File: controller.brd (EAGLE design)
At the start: 100 x 80 mm, 48 parts, among them IC1 7805DT, Q2 MOSFET-NCHANNELBSS123LT1G, Q3 MOSFET-NCHANNELFDD8780, Q5 MMBT4403, SW1 ROT_ENCODER, U1 ATMEGA328P, Y1 16MHz

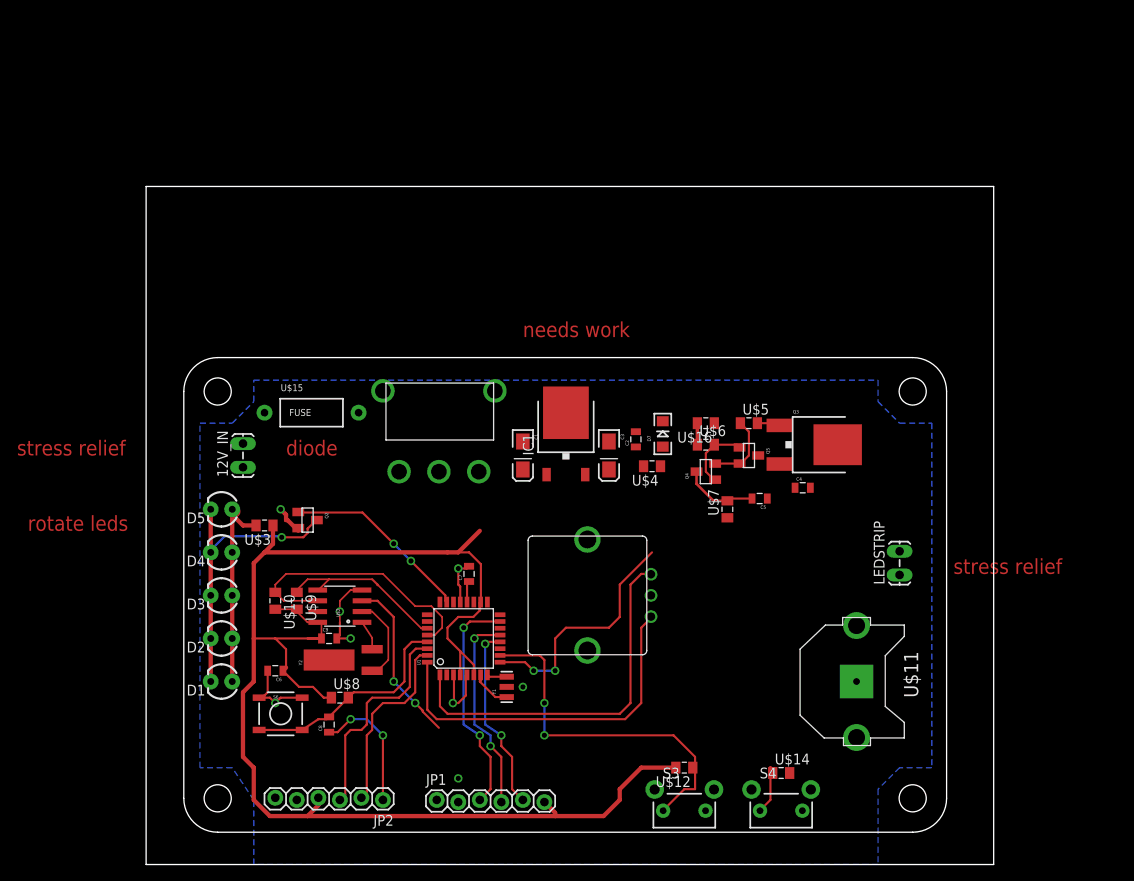
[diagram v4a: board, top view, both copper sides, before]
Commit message: began moving controller to smaller board size.
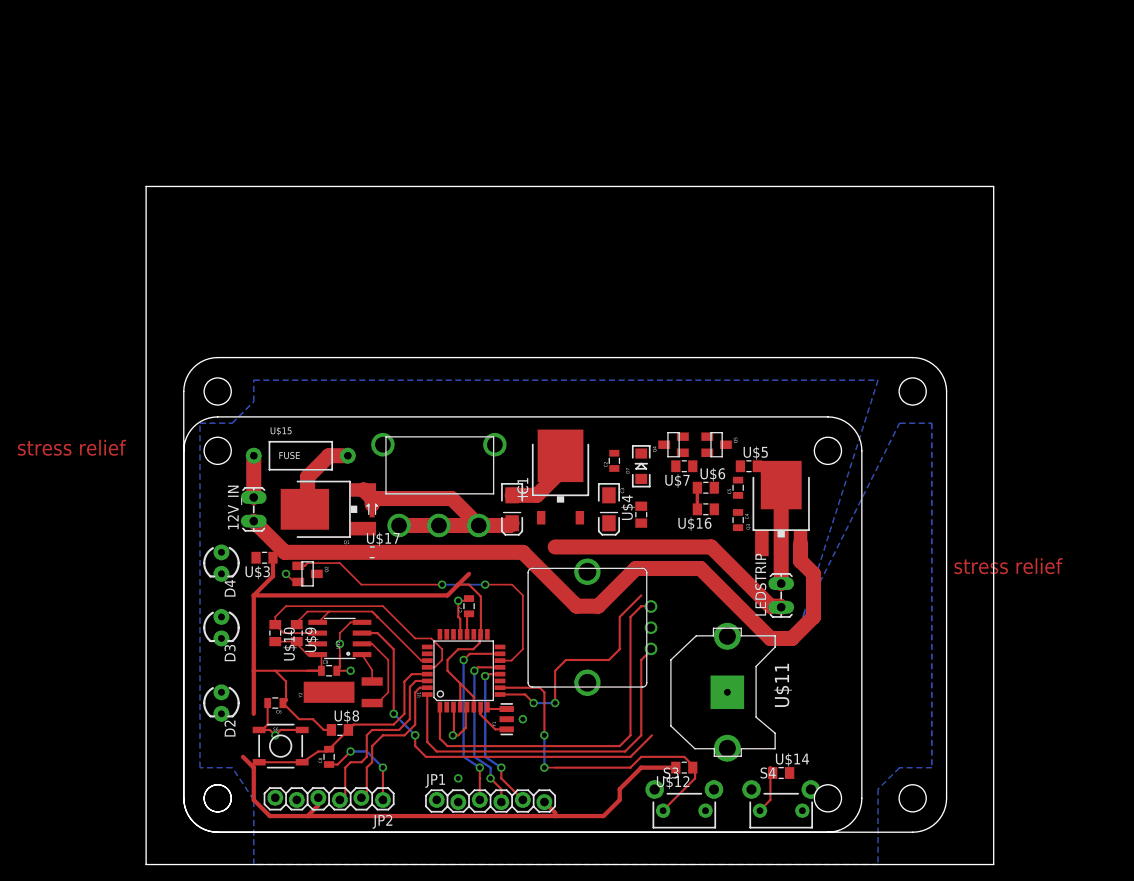
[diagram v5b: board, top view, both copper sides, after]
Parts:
- removed D5: WHITE, SparkFun-LED:LED3MM
- added Q1: MOSFET-PCHANNEL, SparkFun-DiscreteSemi:DPAK
- added U$17: (no value), jt_parts:RESISTOR-0805
- added U$18: (no value), dp_pcb:DP8049_V1
- D1: value WHITE -> DIODE-SCHOTTKY; device SparkFun-LED:LED3MM -> SparkFun-DiscreteSemi:SOD-523
- moved D1 27.0 mm to (26.7, 41.9), turned to 90 degrees
- moved U$11 15.3 mm to (68.6, 20.3)
- moved LEDSTRIP 14.5 mm to (74.9, 30.5)
- moved U$16 10.2 mm to (66.0, 41.9)
- moved C4 8.52 mm to (69.8, 40.6), turned to 270 degrees
- moved Q3 8.13 mm to (74.9, 43.2), turned to 0 degrees
- moved D2 7.62 mm to (8.89, 19.1), turned to 270 degrees
- moved U$7 7.18 mm to (63.5, 47.0), turned to 180 degrees
- moved 12V_IN 6.48 mm to (12.7, 40.6)
- moved C1 6.48 mm to (43.2, 41.9)
- moved C3 6.35 mm to (54.6, 41.9)
- moved Q2 6.35 mm to (19.1, 34.3)
- moved U$13 6.35 mm to (27.9, 49.5)
- moved U$4 5.85 mm to (58.4, 41.3), turned to 90 degrees
- moved U$15 5.24 mm to (19.1, 48.3)
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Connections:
- new net N$13: Q1.4, U$15.P$2
- new net N$14: D1.C, Q1.3, U$13.P$4
- new net N$16: D1.A, Q1.1, U$17.2
- new net N$8: 12V_IN.2, U$15.P$1
- net 12V: no longer 12V_IN.2, U$13.P$4
- net GND: now also U$17.1
- net N$12: no longer D1.K, D5.K
- net N$9: no longer D1.A, D5.A
- net NITE: now also U1.14; no longer U1.23
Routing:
- net GND: track 36.1 -> 127.7 mm
- net 12V: track 0.00 -> 43.1 mm
- net N$12: track 35.0 -> 0.00 mm, vias 1 -> 0
- net VBATT: track 21.2 -> 46.5 mm
- net N$9: track 24.7 -> 0.00 mm
- net N$14: track 0.00 -> 16.1 mm
- net NITE: track 22.3 -> 37.8 mm
- net 12V-RETURN: track 0.00 -> 11.6 mm
- net 5V: track 173.0 -> 162.3 mm
- net N$13: track 0.00 -> 9.92 mm
- net N$2: track 8.93 -> 0.00 mm
- net N$5: track 8.60 -> 0.00 mm
- net NONE: track 8.20 -> 0.00 mm
- net N$8: track 0.00 -> 4.92 mm
- net SCK: track 27.0 -> 22.1 mm
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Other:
- board text removed: "diode"
- board text removed: "needs work"
- board text removed: "rotate leds"

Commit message: removed totem pole, switches, encoder, and disaply board jumper.
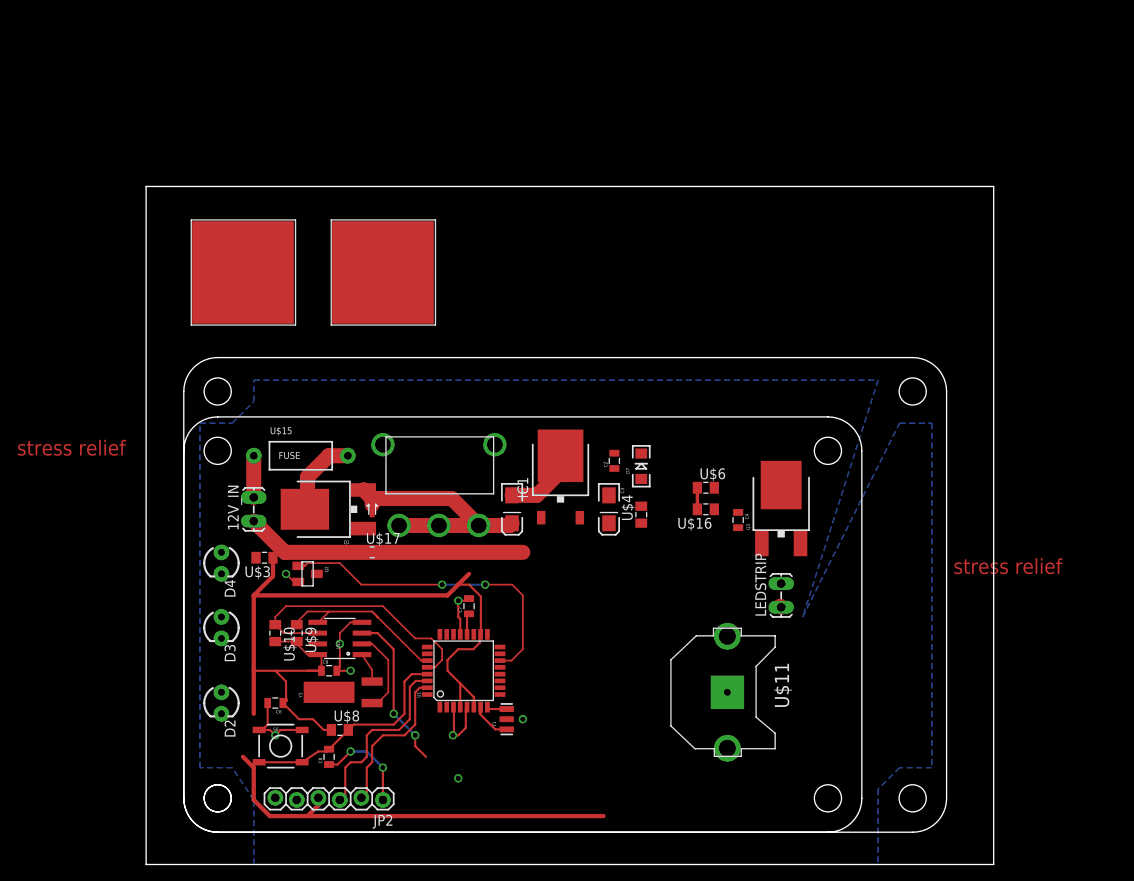
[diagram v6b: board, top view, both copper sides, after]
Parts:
- removed C5: (no value), SparkFun-Capacitors:0805
- removed JP1: (no value), SparkFun-Connectors:1X06_LOCK
- removed Q4: (no value), SparkFun-DiscreteSemi:SOT23
- removed Q5: MMBT4403, SparkFun-DiscreteSemi:SOT23
- removed S3, S4: SWITCH-MOMENTARY-2SIDE_EZ, SparkFun-Electromechanical:TACTILE-PTH-SIDEEZ
- removed SW1: ROT_ENCODER, jt_parts:ROT-ENCODER-EVEGA
- removed U$12, U$14: (no value), jt_parts:RESISTOR-0805
- U$5, U$7: value (none) -> CAPSENSE_PAD; device jt_parts:RESISTOR-0805 -> SparkFun-Electromechanical:CAPSENSE_PAD
- moved U$7 56.9 mm to (11.4, 69.8), turned to 0 degrees
- moved U$5 48.9 mm to (27.9, 69.8)
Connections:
- removed net ENC_A: SW1.P$1, U1.32
- removed net ENC_B: SW1.P$2, U1.1
- removed net N$2: C5.2, Q4.3, U$7.2
- removed net N$5: Q4.2, Q5.2, U$5.1
- removed net RCK: JP1.4, U1.13
- removed net SCK: JP1.3, U1.15
- removed net SERIAL: JP1.5, U1.12
- removed net SW1: S3.1, U$12.1, U1.10
- removed net SW2: S4.1, U$14.1, U1.11
- removed net VCC: U$7.1
- net 5V: no longer JP1.6, U$12.2, U$14.2
- net GND: no longer C5.1, JP1.2, Q5.3, S3.2, S4.2, SW1.P$3
- net N$3: no longer U$5.2
- net NONE: no longer Q4.1, Q5.1
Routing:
- net GND: track 127.7 -> 75.1 mm
- net ENC_B: track 44.0 -> 0.00 mm
- net ENC_A: track 42.8 -> 0.00 mm
- net SW1: track 40.3 -> 0.00 mm, vias 2 -> 0
- net 12V: track 43.1 -> 13.6 mm
- net VBATT: track 46.5 -> 18.8 mm
- net PWM: track 29.3 -> 2.54 mm, vias 2 -> 0
- net SCK: track 22.1 -> 0.00 mm, vias 2 -> 0
- net RCK: track 20.2 -> 0.00 mm, vias 2 -> 0
- net SERIAL: track 18.5 -> 0.00 mm, vias 2 -> 0
- net 5V: track 162.3 -> 148.5 mm
- net 12V-RETURN: track 11.6 -> 0.00 mm
- net SW2: track 5.81 -> 0.00 mm

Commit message: changed to one board design.
 added LCD. added capacitive sense IC. changed to SMD programming
header.
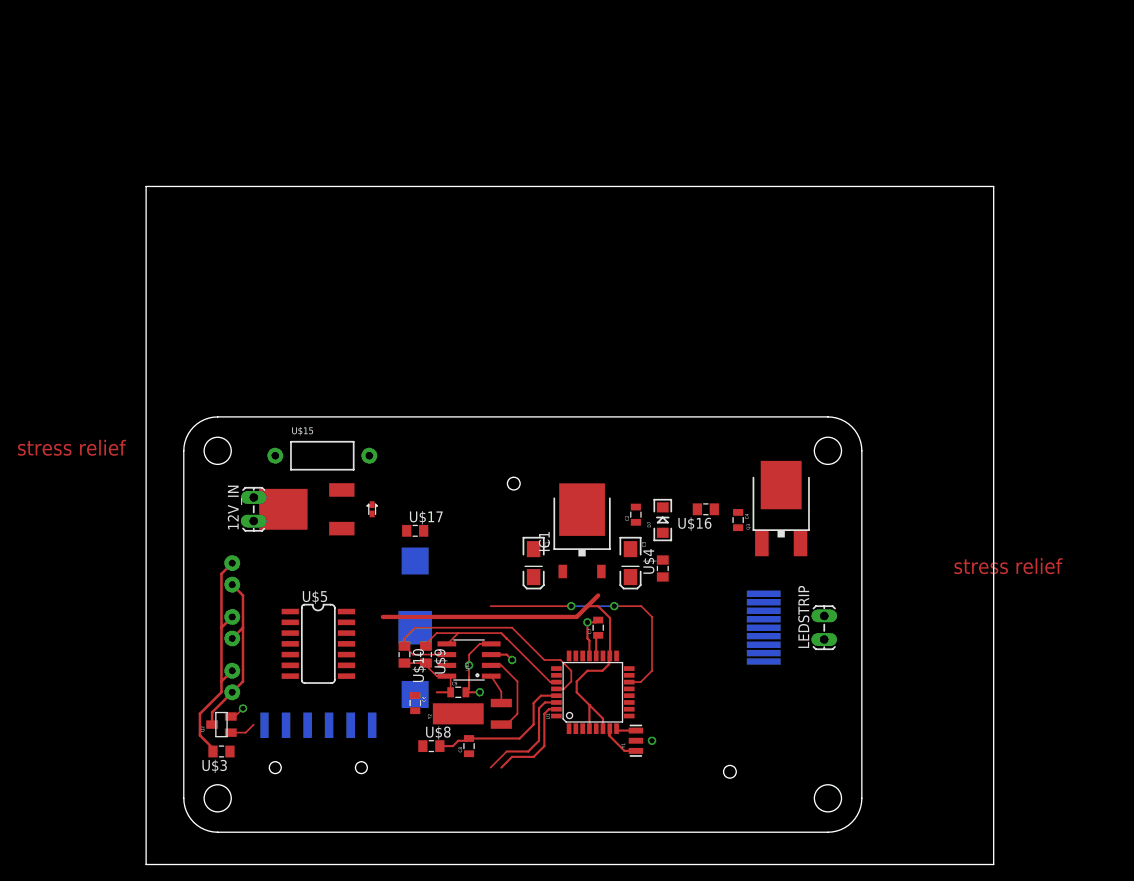
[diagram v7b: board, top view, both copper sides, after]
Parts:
- removed FRAME2: FRAME-LETTER, SparkFun-Aesthetics:CREATIVE_COMMONS
- removed JP2: (no value), SparkFun-Connectors:1X06_LOCK
- removed S6: (no value), SparkFun-Electromechanical:TACTILE_SWITCH_SMD
- removed U$11: (no value), adafruit:CR1220-THM
- removed U$13: SWITCH-SPDT, jt_parts:SWITCH-SPDT-T511006
- removed U$6: (no value), jt_parts:RESISTOR-0805
- removed U$7: CAPSENSE_PAD, SparkFun-Electromechanical:CAPSENSE_PAD
- added BAT1: (no value), SparkFun-Electromechanical:BATTCON_12MM
- added ICP: (no value), SparkFun-Connectors:1X06-SMD
- added NOKIA5110: LPH-7366, lph-7366:LPH-7366
- D1: value DIODE-SCHOTTKY -> (none)
- Q1: value MOSFET-PCHANNEL -> (none); device SparkFun-DiscreteSemi:DPAK -> jt_parts:DPAK
- U$1: value (none) -> FRAME_LETTER; device dp_pcb:DP9056_V1 -> jt_parts:CREATIVE_COMMONS
- U$15: value FUSE -> (none)
- U$5: value CAPSENSE_PAD -> AT42QT1070; device SparkFun-Electromechanical:CAPSENSE_PAD -> jt_parts:SOIC-14
- moved U$5 43.8 mm to (20.3, 26.7), turned to 270 degrees
- moved U$1 24.9 mm to (-15.2, -11.4)
- moved U$3 23.4 mm to (8.89, 13.3)
- moved Q2 20.5 mm to (8.89, 16.5), turned to 90 degrees
- moved C8 16.6 mm to (38.1, 14.0)
- moved C6 16.5 mm to (31.8, 19.1), turned to 270 degrees
- moved U$2 15.5 mm to (38.1, 24.1)
- moved C7 15.5 mm to (53.3, 27.9)
- moved U$9 15.5 mm to (33.0, 24.8)
- moved U$10 15.5 mm to (30.5, 24.8)
- moved C9 15.5 mm to (36.8, 20.3)
- moved U1 15.5 mm to (52.7, 20.3)
- moved Y1 15.5 mm to (57.8, 14.6)
- moved Y2 15.5 mm to (41.9, 17.8)
- moved U$8 11.0 mm to (33.7, 14.0)
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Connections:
- net NITE renamed LIGHT
- removed net NONE: U$6.2
- removed net PWM: U$16.2, U$6.1, U1.9
- new net N$17: NOKIA5110.4
- new net N$18: NOKIA5110.5
- new net N$19: NOKIA5110.9
- new net N$2: NOKIA5110.3
- new net N$20: NOKIA5110.6
- new net N$22: NOKIA5110.8
- new net N$5: NOKIA5110.2
- new net PWM_LED: U$16.2, U1.9
- new net VDD: U$5.13
- new net VSS: U$5.14
- net 12V: no longer C1.A, IC1.1, U$13.P$3, U$13.P$5
- net 5V: now also ICP.4, NOKIA5110.1; no longer JP2.4
- net DTR: now also ICP.1; no longer JP2.1
- net GND: now also BAT1.GND, ICP.5, ICP.6, NOKIA5110.7; no longer JP2.5, JP2.6, S6.1, S6.2, U$11.-
- net N$14: now also C1.A, IC1.1; no longer U$13.P$4
- net N$15: no longer S6.3, S6.4
- net RXI: now also ICP.3; no longer JP2.3
- net TXO: now also ICP.2; no longer JP2.2
- net VBATT: now also BAT1.PWR@1; no longer U$11.+2
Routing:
- net 5V: track 148.5 -> 59.3 mm
- net GND: track 75.1 -> 17.2 mm, vias 8 -> 5
- net N$9: track 0.00 -> 28.0 mm
- net N$12: track 0.00 -> 20.3 mm
- net N$14: track 16.1 -> 0.00 mm
- net VBATT: track 18.8 -> 4.10 mm, vias 2 -> 1
- net 12V: track 13.6 -> 0.00 mm
- net DTR: track 11.6 -> 0.00 mm, vias 2 -> 0
- net N$13: track 9.92 -> 0.00 mm
- net N$15: track 26.2 -> 17.7 mm
- net RXI: track 21.7 -> 13.2 mm
- net TXO: track 18.2 -> 11.6 mm
- net LIGHT: track 37.8 -> 32.3 mm
- net N$8: track 4.92 -> 0.00 mm
- net PWM: track 2.54 -> 0.00 mm
- removed copper zone on layer 16, net GND

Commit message: Layed out new power section. Some new digital routing. Added rt angle SMT LEDs.
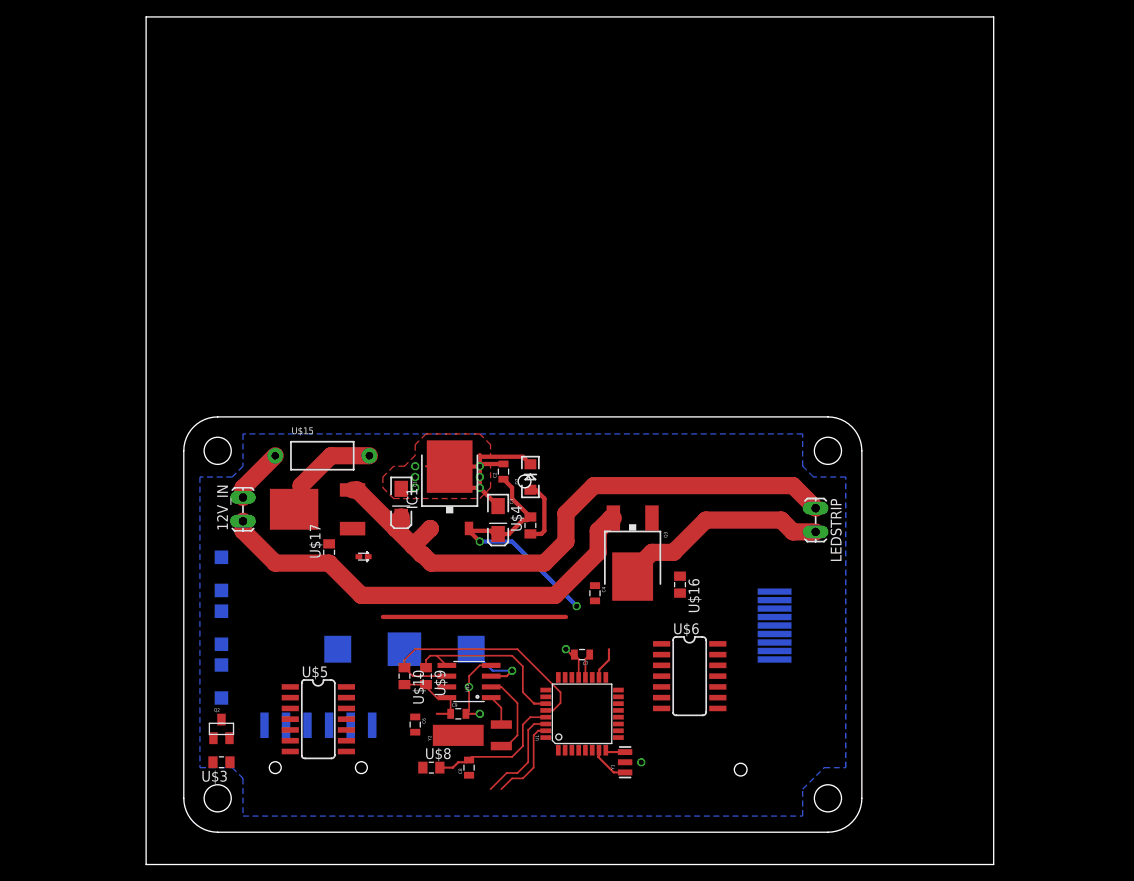
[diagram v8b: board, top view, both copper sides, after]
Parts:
- added U$6: AT42QT1070, jt_parts:SOIC-14
- C1, C3: value (none) -> 10uF
- C2: value (none) -> 0.1uF
- D2, D3, D4: device SparkFun-LED:LED3MM -> adafruit:MICRO-SIDELED
- U$10, U$16, U$17, U$8, U$9: value (none) -> 10k
- moved Q3 19.1 mm to (57.4, 35.6), turned to 180 degrees
- moved C4 19.0 mm to (53.0, 32.0)
- moved C1 17.2 mm to (30.1, 42.7)
- moved D7 16.4 mm to (45.3, 45.7)
- moved IC1 16.4 mm to (35.8, 44.5)
- moved U$4 16.4 mm to (45.3, 40.0)
- moved C2 16.4 mm to (42.2, 46.4)
- moved C3 16.4 mm to (41.5, 40.6)
- moved LEDSTRIP 15.3 mm to (79.0, 41.9), turned to 270 degrees
- moved U$17 10.5 mm to (21.6, 36.8), turned to 90 degrees
- moved U$16 9.40 mm to (63.0, 33.0), turned to 270 degrees
- moved U$5 8.89 mm to (20.3, 17.8)
- moved D1 5.68 mm to (25.7, 36.3), turned to 0 degrees
- moved C7 3.70 mm to (51.4, 24.8), turned to 180 degrees
- moved BAT1 2.84 mm to (30.5, 25.4), turned to 0 degrees
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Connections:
- net 12V-RETURN renamed N$14
- removed net N$14 (its old number): C1.A, D1.C, IC1.1, Q1.3
- removed net N$3: Q3.1
- net 12V: now also C1.A, D1.C, IC1.1, Q1.3
- net N$12: now also D2.C, D3.C, D4.C; no longer D2.K, D3.K, D4.K
- net PWM_LED: now also Q3.1
- net VDD: now also U$6.13
- net VSS: now also U$6.14
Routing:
- net GND: track 17.2 -> 93.9 mm, vias 5 -> 10
- net 12V: track 0.00 -> 69.6 mm
- net LIGHT: track 32.3 -> 0.00 mm, vias 2 -> 0
- net N$9: track 28.0 -> 0.00 mm
- net N$14: track 0.00 -> 25.3 mm
- net N$12: track 20.3 -> 0.00 mm
- net N$13: track 0.00 -> 12.6 mm
- net N$10: track 0.00 -> 7.69 mm
- net N$8: track 0.00 -> 6.50 mm
- net 5V: track 59.3 -> 65.6 mm, vias 0 -> 2
- net VBATT: track 4.10 -> 8.60 mm
- net SCL: track 32.0 -> 30.8 mm
- net RXI: track 13.2 -> 11.9 mm
- net TXO: track 11.6 -> 10.3 mm
- net N$15: track 17.7 -> 16.4 mm
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- added copper zone on layer 1, net GND
- added copper zone on layer 16, net GND
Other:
- board size 100 x 80 mm -> 100 x 100 mm
- board text removed: "stress relief"
